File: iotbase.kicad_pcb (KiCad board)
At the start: 2 copper layers, 57.6 x 72.5 mm, 36 parts, among them J1 USB_C_Receptacle_USB2.0, J2 RCWL-0516, J3 HSPI, J4 VSPI, SW1 Reset, SW2 Boot, U1 AMS1117-3.3, U2 Connector_IoT_GPIO, U3 ESP32-WROOM-E, U4 BME280, U6 Connector_ESProg, U7 Connector_I2C, U8 Connector_I2C

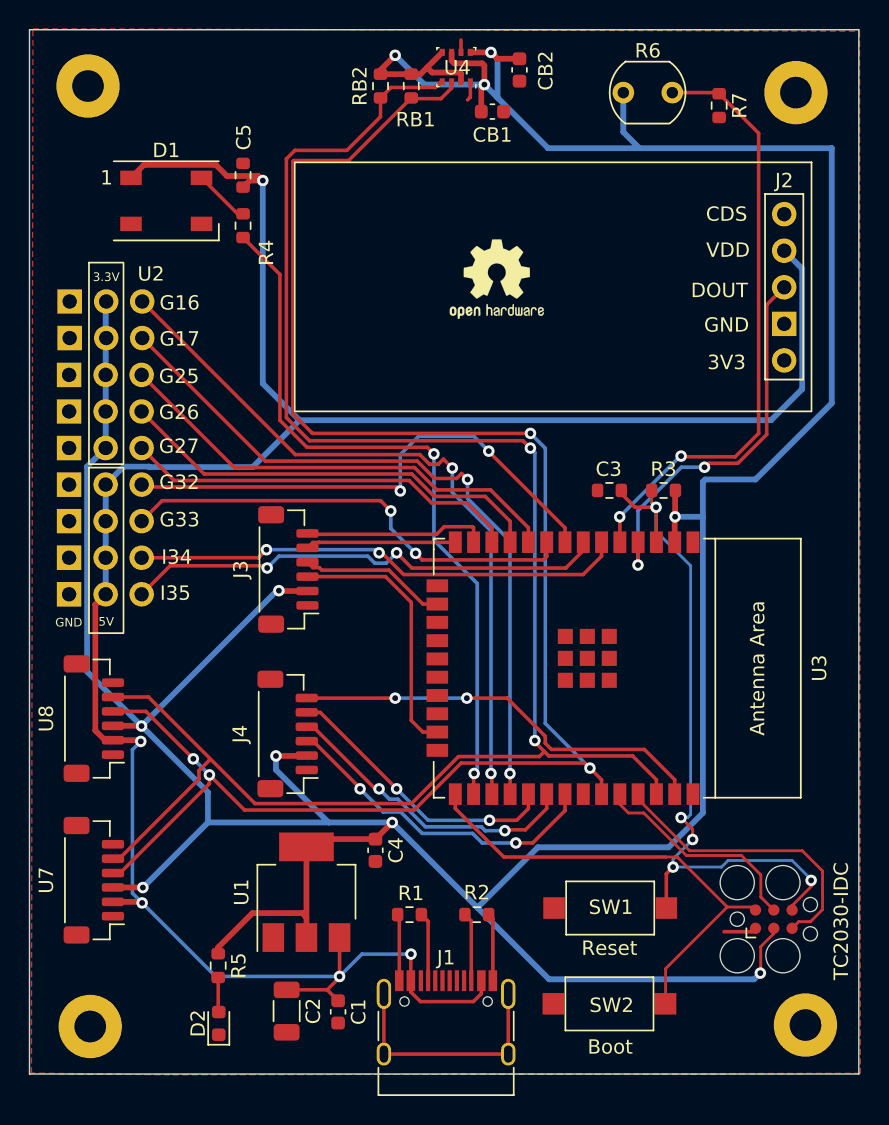
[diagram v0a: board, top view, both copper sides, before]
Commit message: updated components and layout.
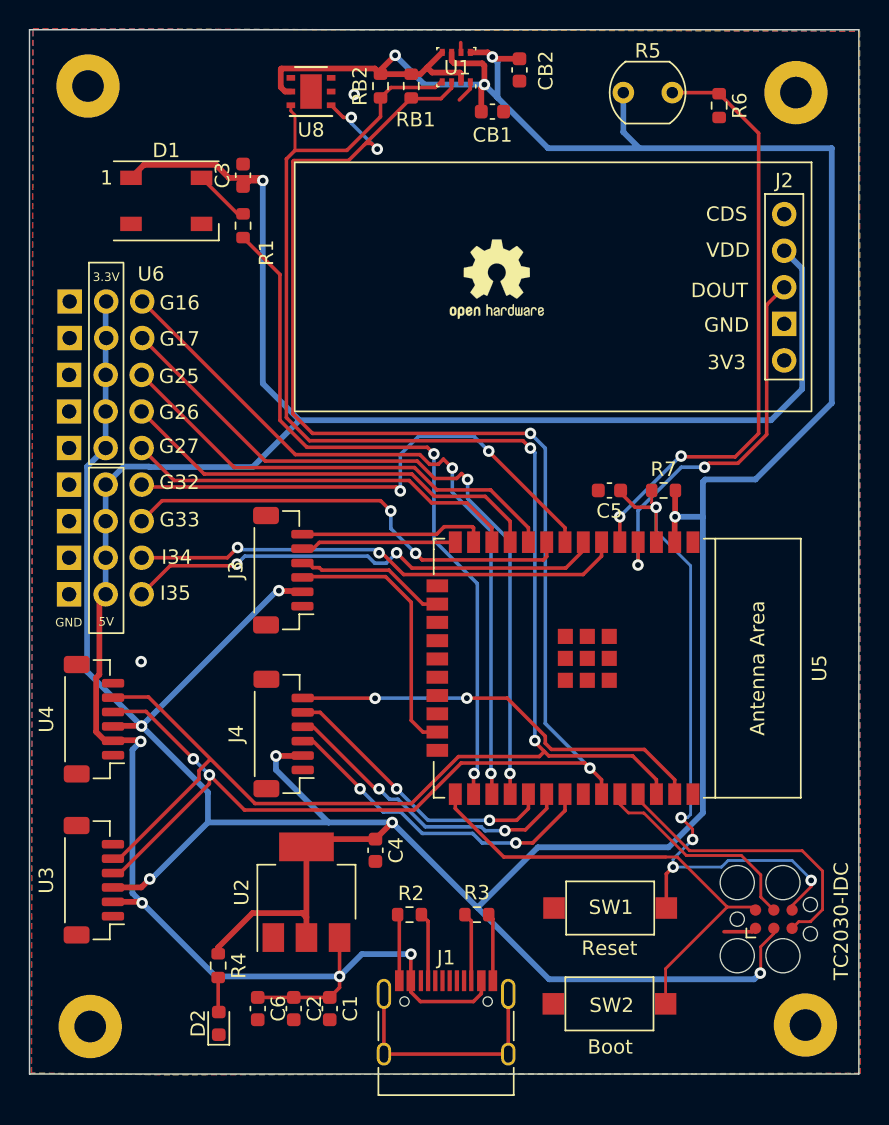
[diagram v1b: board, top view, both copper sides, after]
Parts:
- added C6: 10uF, Capacitor_SMD:C_0603_1608Metric, F.Cu at (104.5, 125.5)
- added U4: Connector_I2C, Connector_JST:JST_SH_BM06B-SRSS-TB_1x06-1MP_P1.00mm_Vertical, F.Cu at (93.1, 105.4)
- C2: value 47uF -> 10uF; footprint Capacitor_SMD:C_1206_3216Metric -> Capacitor_SMD:C_0603_1608Metric
- C3: renamed from C5; footprint Resistor_SMD:R_0603_1608Metric -> Capacitor_SMD:C_0603_1608Metric
- C5: renamed from C3; footprint Resistor_SMD:R_0603_1608Metric -> Capacitor_SMD:C_0603_1608Metric
- CB1, CB2: value 100 nF -> 100nF
- R4: renamed from R5; value 5.1kΩ -> 4k7
- U8: value Connector_I2C -> HDC1080; footprint Connector_JST:JST_SH_BM06B-SRSS-TB_1x06-1MP_P1.00mm_Vertical -> Package_SON:Texas_PWSON-N6
- moved U8 46.1 mm to (108.2, 61.8), turned to 180 degrees
- moved C1 0.63 mm to (109.5, 125.5)
- moved C2 0.52 mm to (107.0, 125.5)
- moved J3 0.36 mm to (106.3, 95.0)
- moved J4 0.28 mm to (106.3, 106.4)
- renumbered R4 to R1, R1 to R2, R2 to R3, R6 to R5, R7 to R6, R3 to R7, U4 to U1, U1 to U2, U7 to U3, U3 to U5, U2 to U6, U6 to U7
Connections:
- J3 pad MP: (no net) -> GND
- J4 pad MP: (no net) -> GND
- U3 pad MP: unconnected-(U7-PadMP) -> GND
- U8 pad 1: GND -> SDA
- U8 pad 2: VBUS -> GND
- U8 pad 3: +3V3 -> unconnected-(U8-Pad3)
- U8 pad 4: SDA -> unconnected-(U8-Pad4)
- U8 pad 5: SCL -> +3V3
- U8 pad 6: GND -> SCL
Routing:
- net +3V3: track 276.9 -> 285.7 mm
- net SDA: track 122.1 -> 127.7 mm, vias 4 -> 6
- net SCL: track 124.6 -> 127.9 mm
- net VBUS: track 162.9 -> 164.0 mm
- net GND: vias 0 -> 2
- added copper zone on B.Cu, net GND

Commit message: adds rounded corners adds connector pin silkscreens
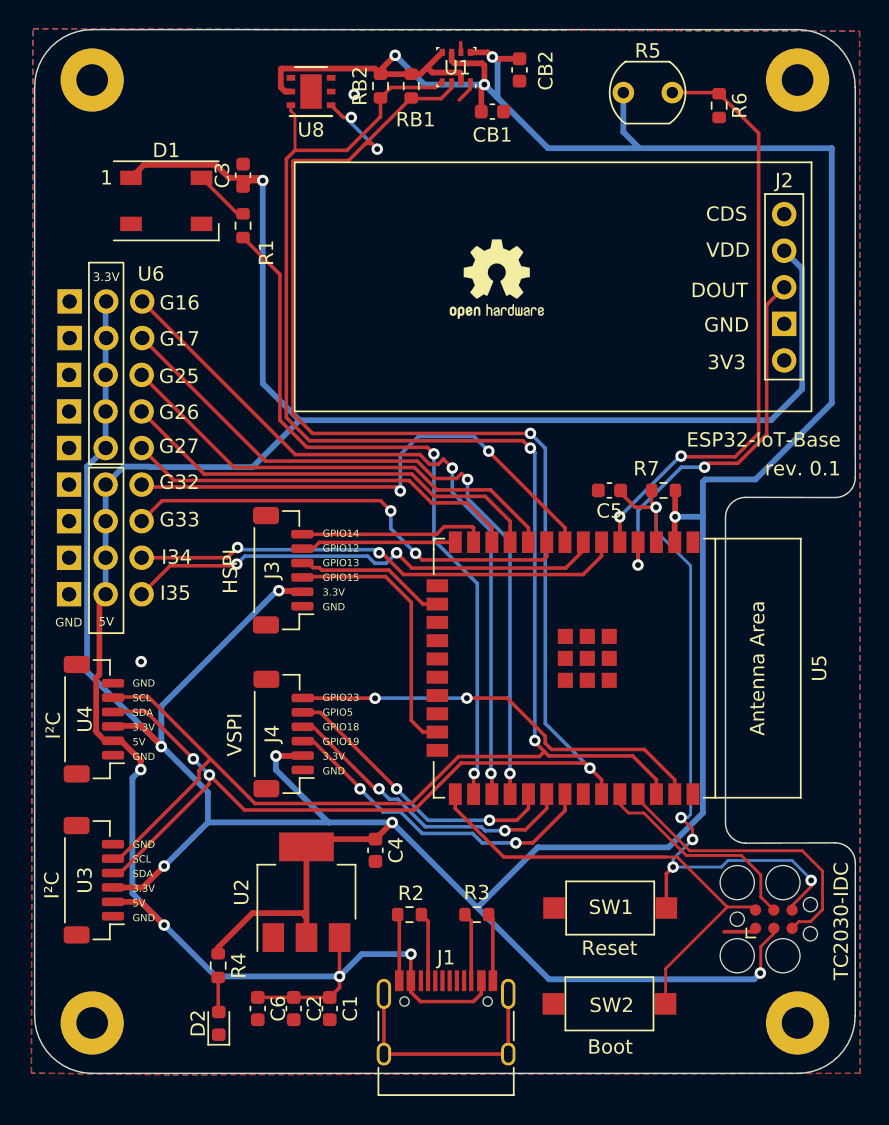
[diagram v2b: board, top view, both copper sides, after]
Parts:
- moved H2 0.88 mm to (142.0, 61.0)
- moved H3 0.56 mm to (142.0, 126.5)
- moved H1 0.51 mm to (93.0, 61.0)
- moved H4 0.28 mm to (93.0, 126.5)
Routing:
- net +3V3: track 285.7 -> 288.6 mm
- net VBUS: track 164.0 -> 165.4 mm
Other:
- board size 57.6 x 72.5 mm -> 57 x 72.5 mm
- board text added: "3.3V"
- board text added: "5V"
- board text added: "ESP32-IoT-Base"
- board text added: "GND"
- board text added: "GPIO12"
- board text added: "GPIO13"
- board text added: "GPIO14"
- board text added: "GPIO15"
- board text added: "GPIO18"
- board text added: "GPIO19"
- board text added: "GPIO23"
- board text added: "GPIO5"
- board text added: "HSPI"
- board text added: "I²C"
- board text added: "SCL"
- board text added: "SDA"
- board text added: "VSPI"
- board text added: "rev. 0.1"

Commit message: updates antenna area cutout adds jlcpcb label
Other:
- outline, holes or cut-outs redrawn
- board text added: "JLCJLCJLCJLC"
- board text added: "© 2022 @mightea @gamule"
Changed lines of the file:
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@@
     (property "Sheetfile" "iotbase.kicad_sch")
     (property "Sheetname" "")
-    (attr smd exclude_from_pos_files)
+    (attr smd)
     (fp_text reference "SW2" (at 0.1524 0.1016) (layer "F.SilkS")
       (effects (font (size 1 1) (thickness 0.15)))
@@
   )
   (gr_arc (start 89 61.5) (mid 90.171573 58.671573) (end 93 57.5) (layer "Edge.Cuts") (width 0.1))
-  (gr_line (start 138.389949 89.989949) (end 144.610051 90) (layer "Edge.Cuts") (width 0.1))
-  (gr_line (start 144.610051 113.989949) (end 138.389949 114.010051) (layer "Edge.Cuts") (width 0.1))
+  (gr_line (start 138.389949 90) (end 144.610051 90) (layer "Edge.Cuts") (width 0.1))
+  (gr_line (start 144.610051 113.7) (end 138.389949 113.7) (layer "Edge.Cuts") (width 0.1))
   (gr_arc (start 93 130) (mid 90.171573 128.828427) (end 89 126) (layer "Edge.Cuts") (width 0.1))
   (gr_line (start 93 130) (end 142 130) (layer "Edge.Cuts") (width 0.1))
@@
   (gr_arc (start 146.010051 88.6) (mid 145.6 89.589949) (end 144.610051 90) (layer "Edge.Cuts") (width 0.1))
   (gr_arc (start 142 57.5) (mid 144.828427 58.671573) (end 146 61.5) (layer "Edge.Cuts") (width 0.1))
-  (gr_arc (start 138.389949 114.010051) (mid 137.4 113.6) (end 136.989949 112.610051) (layer "Edge.Cuts") (width 0.1))
+  (gr_arc (start 138.389949 113.7) (mid 137.400014 113.289935) (end 136.989949 112.3) (layer "Edge.Cuts") (width 0.1))
   (gr_arc (start 146 126) (mid 144.828427 128.828427) (end 142 130) (layer "Edge.Cuts") (width 0.1))
-  (gr_arc (start 144.610051 113.989949) (mid 145.6 114.4) (end 146.010051 115.389949) (layer "Edge.Cuts") (width 0.1))
+  (gr_arc (start 144.610051 113.689949) (mid 145.599986 114.100014) (end 146.010051 115.089949) (layer "Edge.Cuts") (width 0.1))
   (gr_line (start 93 57.5) (end 142 57.5) (layer "Edge.Cuts") (width 0.1))
   (gr_line (start 89 61.5) (end 89 126) (layer "Edge.Cuts") (width 0.1))
-  (gr_line (start 146 126) (end 146.010051 115.389949) (layer "Edge.Cuts") (width 0.1))
-  (gr_line (start 136.989949 112.610051) (end 136.989949 91.389949) (layer "Edge.Cuts") (width 0.1))
+  (gr_line (start 146 126) (end 146.010051 115.089949) (layer "Edge.Cuts") (width 0.1))
+  (gr_line (start 136.989949 112.3) (end 136.989949 91.389949) (layer "Edge.Cuts") (width 0.1))
   (gr_line (start 146.010051 88.6) (end 146 61.5) (layer "Edge.Cuts") (width 0.1))
+  (gr_text "© 2022\n@mightea\n@gamule " (at 134.6 127.5) (layer "F.SilkS")
+    (effects (font (size 0.5 0.5) (thickness 0.1)) (justify left))
+  )
   (gr_text "GPIO13" (at 109 94.54) (layer "F.SilkS")
     (effects (font (size 0.5 0.5) (thickness 0.1)) (justify left))
@@
     (effects (font (size 0.5 0.5) (thickness 0.1)) (justify left))
   )
+  (gr_text "JLCJLCJLCJLC" (at 132.1 101.2 90) (layer "F.SilkS")
+    (effects (font (size 1 1) (thickness 0.15)))
+  )
   (gr_text "SCL" (at 95.8 115.12) (layer "F.SilkS")
     (effects (font (size 0.5 0.5) (thickness 0.1)) (justify left))
@@
     (effects (font (size 0.5 0.5) (thickness 0.1)) (justify left))
   )
-  (gr_text "TC2030-IDC" (at 145.034 119.4308 90) (layer "F.SilkS")
+  (gr_text "TC2030-IDC" (at 144.5 119.3 90) (layer "F.SilkS")
     (effects (font (size 1 1) (thickness 0.15)))
   )
@@
     )
   )
-  (zone (net 0) (net_name "") (layers F&B.Cu) (name "Antenna Area") (hatch edge 0.508)
-    (connect_pads (clearance 0))
-    (min_thickness 0.254)
-    (keepout (tracks not_allowed) (vias not_allowed) (pads not_allowed ) (copperpour not_allowed) (footprints not_allowed))
-    (fill (thermal_gap 0.508) (thermal_bridge_width 0.508))
-    (polygon
-      (pts
-        (xy 146.10526 114.436373)
-        (xy 135.957389 114.39037)
-        (xy 135.9526 89.2556)
-        (xy 146.049671 89.250803)
-      )
-    )
-  )
   (group "" (id 9204341d-1be4-4239-aa20-6c9f2e3cec64)
     (members
@@
     )
   )
-  (group "" (id e59fb6ac-8fc7-4587-98c4-4f73f20fb5c2)
-    (members
-      f240e733-157e-4a15-812f-78f42d8a8322
-    )
-  )
